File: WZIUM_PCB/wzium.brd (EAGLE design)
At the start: 160 x 100 mm, 15 parts, among them J1 RASPBERRYPI-40-PIN-GPIO_PTH

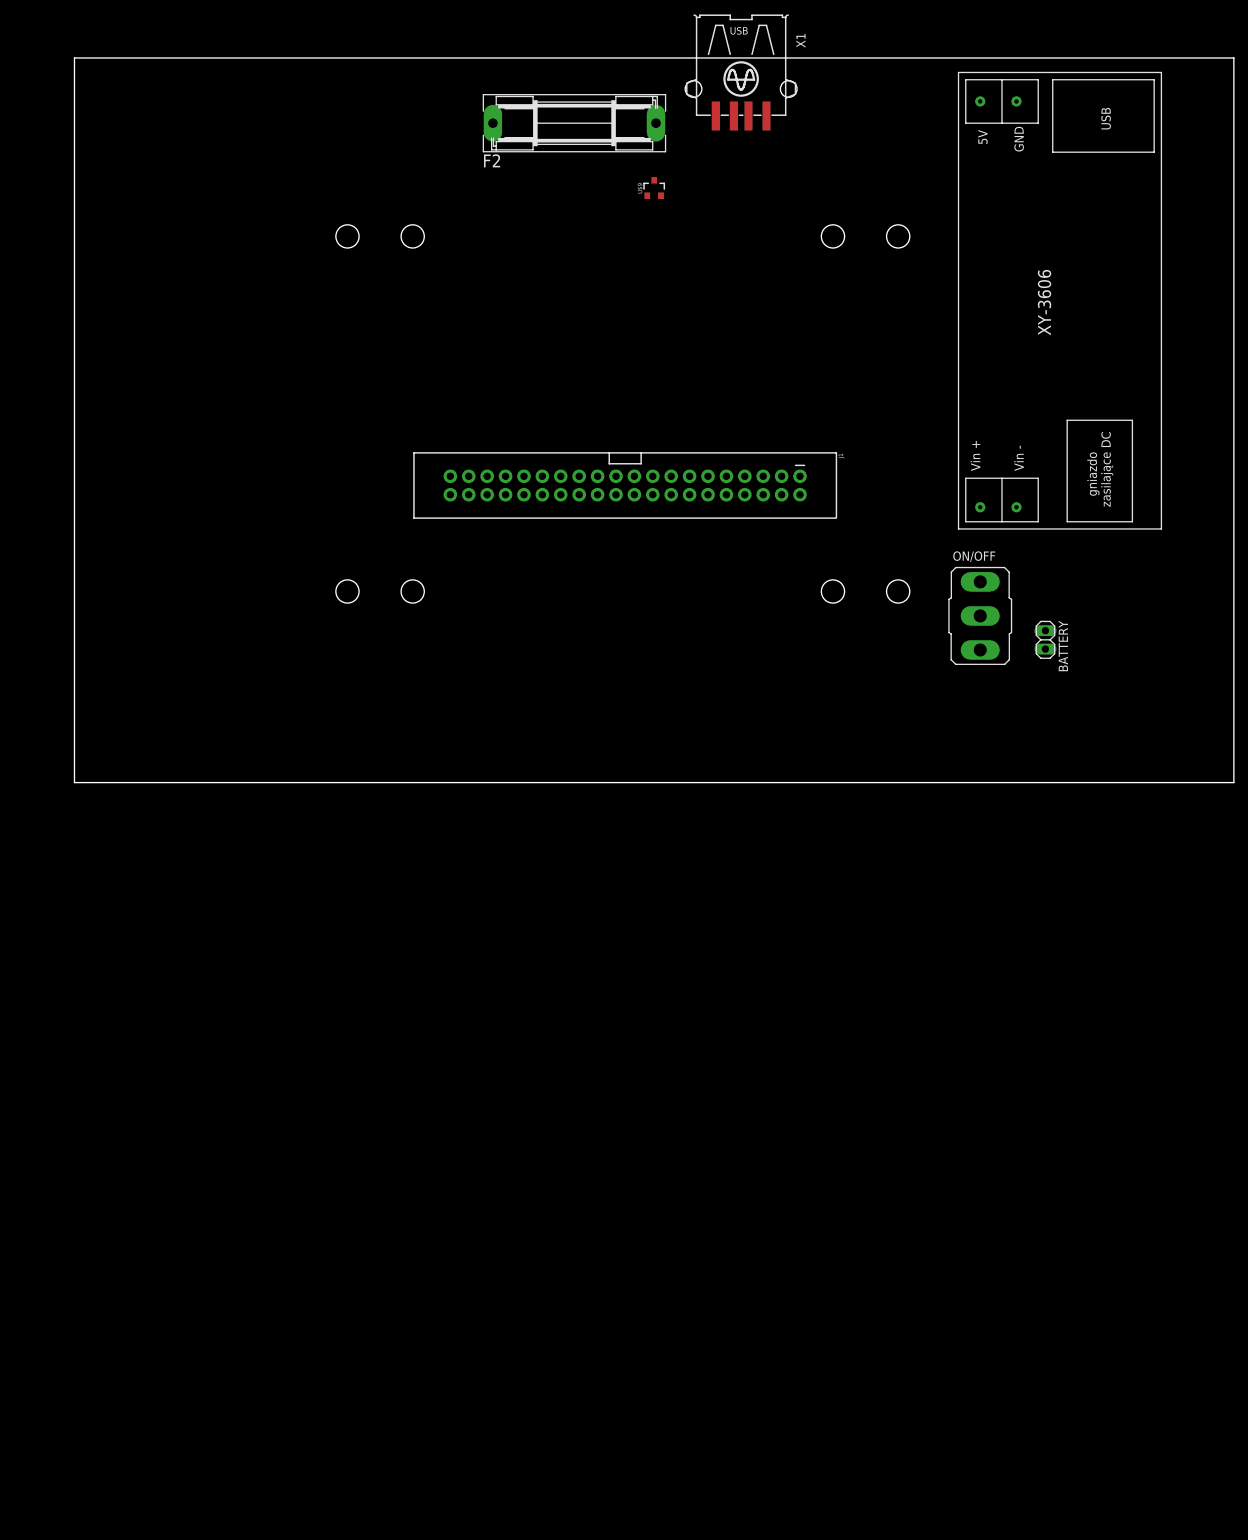
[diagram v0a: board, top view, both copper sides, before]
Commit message: [PCB] Zmieniono wielkość płytki na 10x10
Docelowo myślimy o JLC PCB, więc przeanalizowałem ich ceny:
-> 2.2 $ za płytkę 10x10 cm
-> 8.8 $ za płytkę 10x12 cm
Spróbujmy zmieścić się na płytce 10x10. Jeśli to niemożliwe to zmienimy rozmiar. Duże moduły można zamontować na podwoziu obok płytki ze sterownikiem i połączyć kablami.
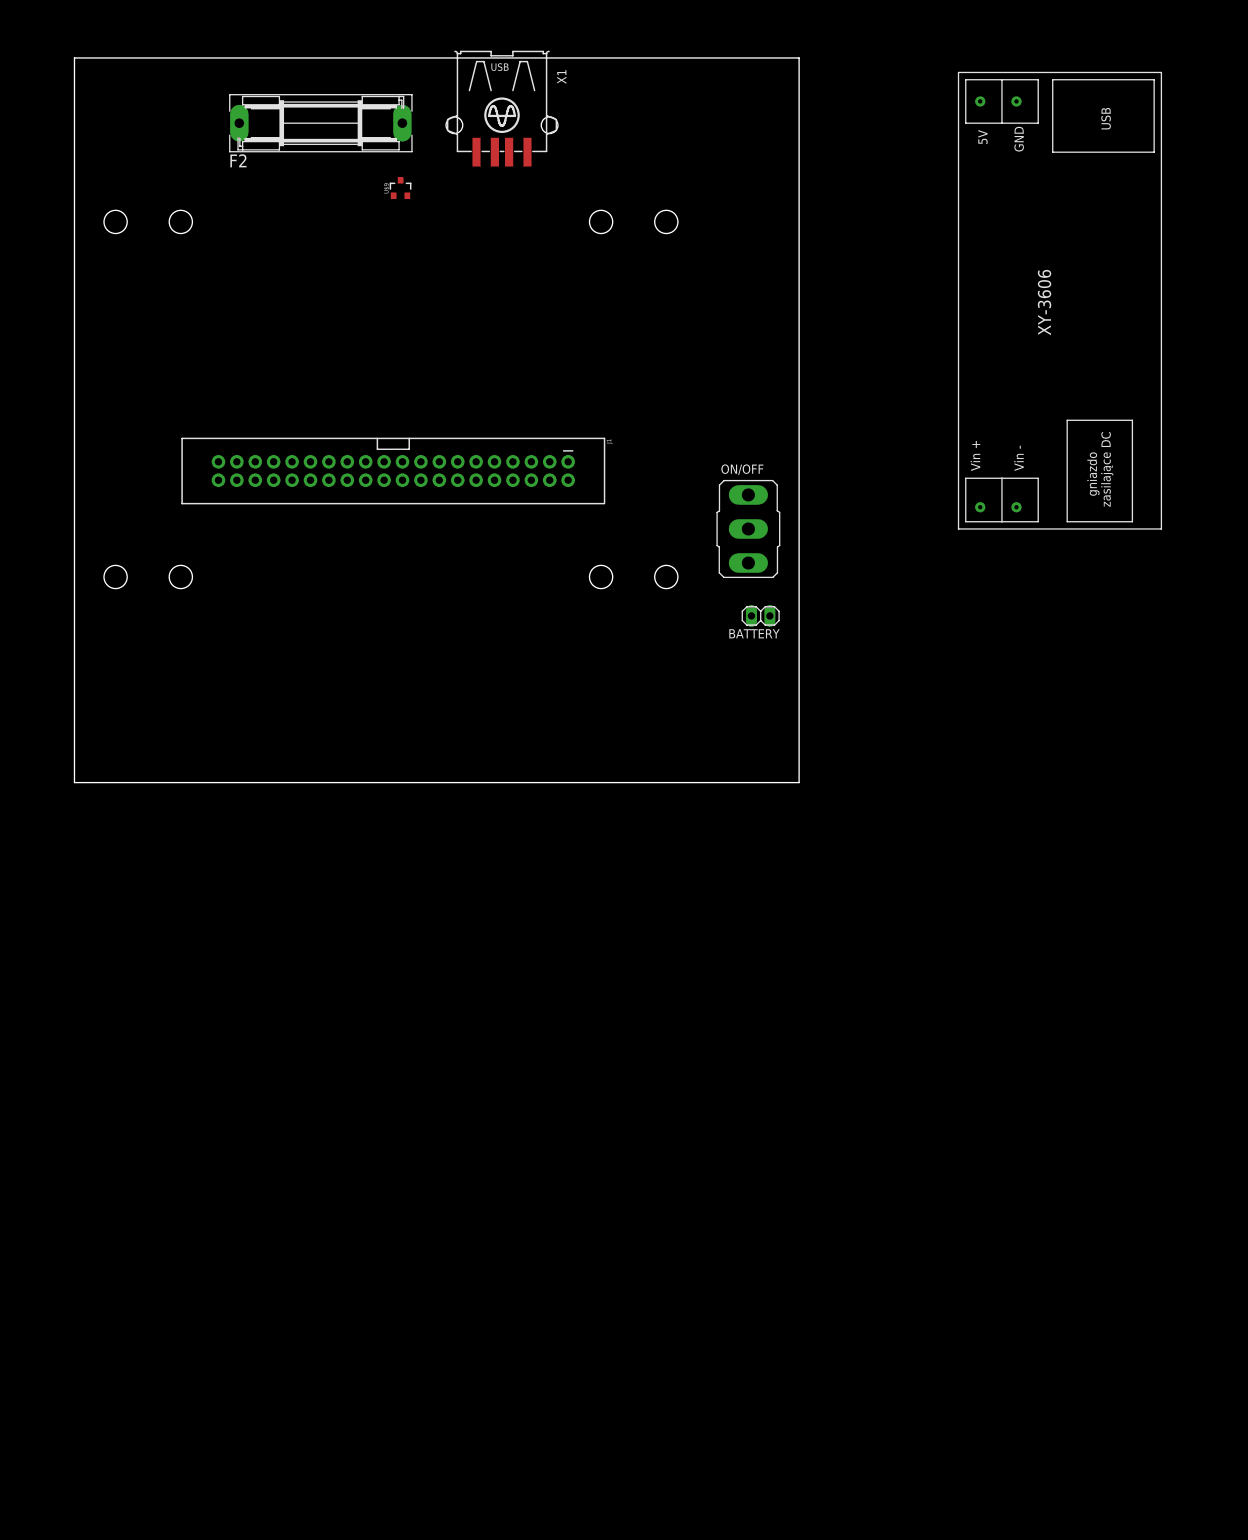
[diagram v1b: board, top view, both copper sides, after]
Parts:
- moved BATTERY 39.4 mm to (94.7, 23.0), turned to 180 degrees
- moved F2 35.0 mm to (34.0, 91.0)
- moved U$9 35.0 mm to (45.0, 82.0)
- moved ON/OFF 34.2 mm to (93.0, 35.0)
- moved X1 33.4 mm to (59.0, 101.0)
- moved J1 32.1 mm to (44.0, 43.0)
- moved U$3 32.1 mm to (72.7, 77.4)
- moved U$4 32.1 mm to (72.7, 28.4)
- moved U$7 32.1 mm to (81.7, 28.4)
- moved U$8 32.1 mm to (81.7, 77.4)
- moved U$1 32.1 mm to (14.7, 28.4)
- moved U$2 32.1 mm to (14.7, 77.4)
- moved U$5 32.1 mm to (5.67, 28.4)
- moved U$6 32.1 mm to (5.67, 77.4)
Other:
- board size 160 x 100 mm -> 100 x 100 mm

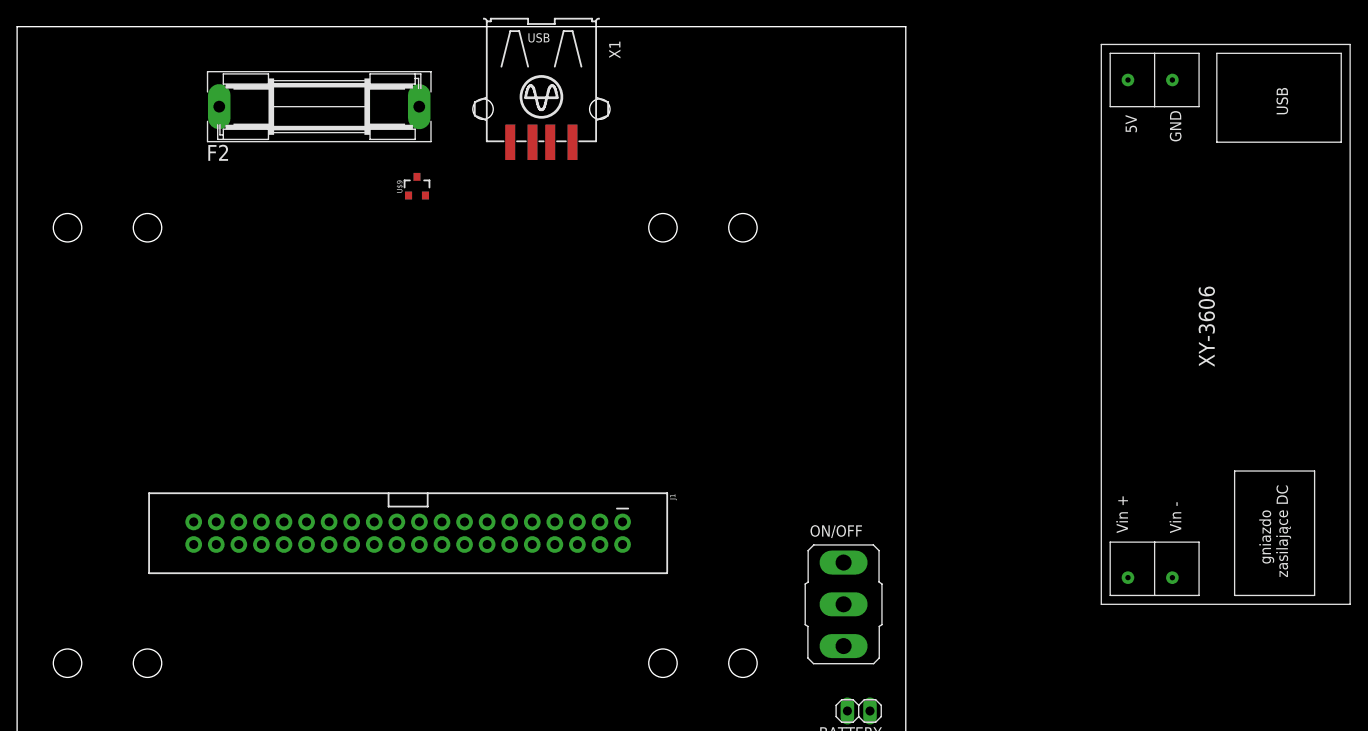
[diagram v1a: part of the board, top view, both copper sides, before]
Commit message: [PCB] Upgraded to EAGLE 9.6.2 i dodano biblioteki
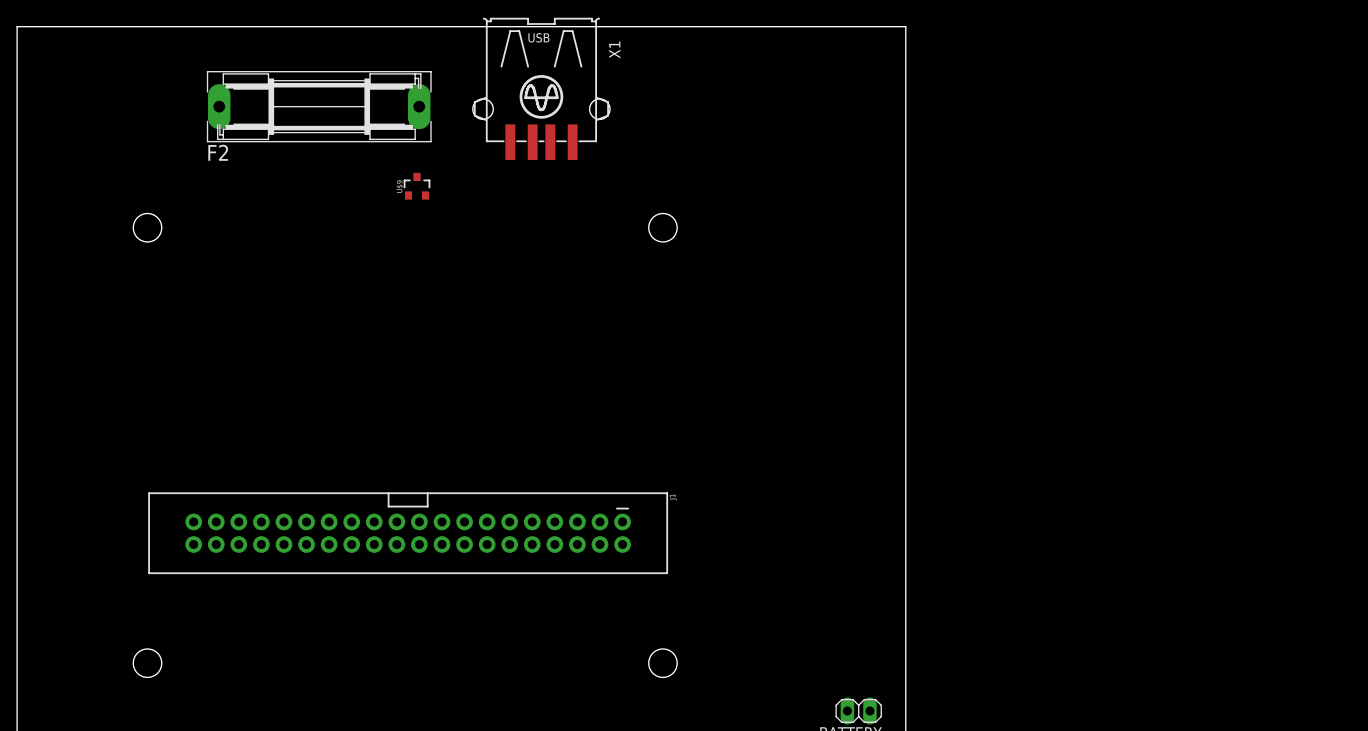
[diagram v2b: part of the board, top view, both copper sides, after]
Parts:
- removed ON/OFF: (no value), gm-switches:M9040P
- removed U$10: XY-3606, _MY_voltage_converters:CONVERTER_DC_TO_5V_DC
- removed U$2, U$6, U$7, U$8: (no value), WingTechCorner:M3-HOLE
- U$1, U$3, U$4, U$5: device WingTechCorner:M3-HOLE -> _MOUNTING_HOLES:M3-HOLE
- moved U$1 58.0 mm to (72.7, 28.4)
- moved U$3 58.0 mm to (14.7, 77.4)
- moved U$4 49.0 mm to (72.7, 77.4)
- moved U$5 9.00 mm to (14.7, 28.4)
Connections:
- removed net N$1: BATTERY.2, ON/OFF.3
- net 5V: no longer U$10.P$3
- net 6V: now also BATTERY.2; no longer ON/OFF.2, U$10.P$1
- net GND: no longer U$10.P$2, U$10.P$4
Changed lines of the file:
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@@
 <?xml version="1.0" encoding="utf-8"?>
 <!DOCTYPE eagle SYSTEM "eagle.dtd">
-<eagle version="9.4.2">
+<eagle version="9.6.2">
 <drawing>
 <settings>
@@
 <wire x1="100" y1="100" x2="0" y2="100" width="0" layer="20"/>
 <wire x1="0" y1="100" x2="0" y2="0" width="0" layer="20"/>
-<dimension x1="8.675" y1="28.3" x2="11.675" y2="28.3" x3="10.175" y3="17.325" textsize="0.3048" layer="1" dtype="horizontal" width="0.05"/>
-<dimension x1="13.075" y1="28.325" x2="16.275" y2="28.325" x3="14.675" y3="17.375" textsize="0.3048" layer="1" dtype="horizontal" width="0.05"/>
-<dimension x1="16.275" y1="28.375" x2="71.075" y2="28.45" x3="43.675" y3="23" textsize="0.4064" layer="1" dtype="horizontal" width="0.05"/>
-<dimension x1="14.675" y1="28.375" x2="72.675" y2="28.4" x3="43.675" y3="20" textsize="0.4064" layer="1" dtype="horizontal" width="0.05"/>
-<dimension x1="14.675" y1="77.375" x2="14.725" y2="28.375" x3="-2" y3="52.875" textsize="0.4064" layer="1" dtype="vertical" width="0.05"/>
-<dimension x1="5.675" y1="75.775" x2="5.675" y2="30.075" x3="1" y3="52.925" textsize="0.4064" layer="1" dtype="vertical" width="0.05"/>
+<dimension x1="17.675" y1="28.3" x2="11.675" y2="28.3" x3="14.675" y3="14.325" textsize="0.6096" layer="1" dtype="horizontal" width="0.05"/>
+<dimension x1="13.075" y1="28.325" x2="16.275" y2="28.325" x3="14.675" y3="17.375" textsize="0.6096" layer="1" dtype="horizontal" width="0.05"/>
+<dimension x1="16.275" y1="28.375" x2="71.075" y2="28.45" x3="43.675" y3="23" textsize="0.6096" layer="1" dtype="horizontal" width="0.05"/>
+<dimension x1="14.675" y1="28.375" x2="72.675" y2="28.4" x3="43.675" y3="20" textsize="0.6096" layer="1" dtype="horizontal" width="0.05"/>
+<dimension x1="14.675" y1="77.375" x2="14.725" y2="28.375" x3="-2" y3="52.875" textsize="1.016" layer="1" dtype="vertical" width="0.05"/>
+<dimension x1="14.8" y1="75.775" x2="14.7" y2="29.975" x3="2" y3="52.875" textsize="1.016" layer="1" dtype="vertical" width="0.05"/>
 </plain>
 <attributes>
@@
 </autorouter>
 <elements>
-<element name="U$1" library="WingTechCorner" package="M3-HOLE" value="" x="14.675" y="28.375" smashed="yes"/>
-<element name="U$2" library="WingTechCorner" package="M3-HOLE" value="" x="14.675" y="77.375" smashed="yes"/>
-<element name="U$3" library="WingTechCorner" package="M3-HOLE" value="" x="72.675" y="77.375" smashed="yes"/>
-<element name="U$4" library="WingTechCorner" package="M3-HOLE" value="" x="72.675" y="28.375" smashed="yes"/>
 <element name="J1" library="SparkFun-Connectors" library_urn="urn:adsk.eagle:library:513" package="2X20_SHROUDED" package3d_urn="urn:adsk.eagle:package:38279/1" value="RASPBERRYPI-40-PIN-GPIO_PTH" x="44" y="43" smashed="yes" rot="R270">
 <attribute name="NAME" x="73.464" y="47.445" size="0.6096" layer="25" font="vector" ratio="20" rot="R270"/>
@@
 <attribute name="VALUE" x="13.901" y="47.318" size="0.6096" layer="27" font="vector" ratio="20" rot="R270"/>
 </element>
-<element name="U$5" library="WingTechCorner" package="M3-HOLE" value="" x="5.675" y="28.375" smashed="yes"/>
-<element name="U$6" library="WingTechCorner" package="M3-HOLE" value="" x="5.675" y="77.375" smashed="yes"/>
-<element name="U$7" library="WingTechCorner" package="M3-HOLE" value="" x="81.675" y="28.375" smashed="yes"/>
-<element name="U$8" library="WingTechCorner" package="M3-HOLE" value="" x="81.675" y="77.375" smashed="yes"/>
 <element name="X1" library="con-yamaichi" library_urn="urn:adsk.eagle:library:202" package="USB-A003" package3d_urn="urn:adsk.eagle:package:11805/1" value="" x="59" y="101" smashed="yes" rot="R180">
 <attribute name="MF" value="" x="59" y="101" size="1.778" layer="27" rot="R180" display="off"/>
@@
 <attribute name="VALUE" x="97.24" y="26.175" size="1.27" layer="27" rot="R180"/>
 </element>
-<element name="ON/OFF" library="gm-switches" package="M9040P" value="" x="93" y="35" smashed="yes">
-<attribute name="NAME" x="89.19" y="42.62" size="1.27" layer="25" ratio="10"/>
-<attribute name="VALUE" x="89.19" y="25.475" size="1.27" layer="27" ratio="10"/>
-</element>
-<element name="U$10" library="_MY_voltage_converters" package="CONVERTER_DC_TO_5V_DC" value="XY-3606" x="150" y="35" smashed="yes" rot="R90"/>
+<element name="U$5" library="_MOUNTING_HOLES" package="M3-HOLE" value="" x="14.675" y="28.375" smashed="yes"/>
+<element name="U$1" library="_MOUNTING_HOLES" package="M3-HOLE" value="" x="72.675" y="28.375" smashed="yes"/>
+<element name="U$4" library="_MOUNTING_HOLES" package="M3-HOLE" value="" x="72.675" y="77.375" smashed="yes"/>
+<element name="U$3" library="_MOUNTING_HOLES" package="M3-HOLE" value="" x="14.675" y="77.375" smashed="yes"/>
 </elements>
 <signals>
@@
 <contactref element="U$9" pad="1"/>
 <contactref element="BATTERY" pad="1"/>
-<contactref element="U$10" pad="P$2"/>
 <contactref element="X1" pad="1"/>
-<contactref element="U$10" pad="P$4"/>
-<wire x1="57.97" y1="44.27" x2="62.5" y2="87" width="0" layer="19" extent="1-1"/>
-<wire x1="63.05" y1="41.73" x2="57.97" y2="44.27" width="0" layer="19" extent="1-1"/>
-<wire x1="52.89" y1="41.73" x2="57.97" y2="44.27" width="0" layer="19" extent="1-1"/>
-<wire x1="45.27" y1="41.73" x2="52.89" y2="41.73" width="0" layer="19" extent="1-1"/>
-<wire x1="37.65" y1="44.27" x2="45.27" y2="41.73" width="0" layer="19" extent="1-1"/>
+<wire x1="44.05" y1="81" x2="62.5" y2="87" width="0" layer="19" extent="1-1"/>
+<wire x1="37.65" y1="44.27" x2="44.05" y2="81" width="0" layer="19" extent="1-1"/>
 <wire x1="32.57" y1="41.73" x2="37.65" y2="44.27" width="0" layer="19" extent="1-1"/>
 <wire x1="27.49" y1="41.73" x2="32.57" y2="41.73" width="0" layer="19" extent="1-1"/>
+<wire x1="45.27" y1="41.73" x2="37.65" y2="44.27" width="0" layer="19" extent="1-1"/>
+<wire x1="52.89" y1="41.73" x2="45.27" y2="41.73" width="0" layer="19" extent="1-1"/>
+<wire x1="57.97" y1="44.27" x2="52.89" y2="41.73" width="0" layer="19" extent="1-1"/>
+<wire x1="63.05" y1="41.73" x2="57.97" y2="44.27" width="0" layer="19" extent="1-1"/>
 <wire x1="19.87" y1="44.27" x2="27.49" y2="41.73" width="0" layer="19" extent="1-1"/>
-<wire x1="130" y1="94" x2="27.49" y2="41.73" width="0" layer="19" extent="1-1"/>
-<wire x1="95.97" y1="23" x2="130" y2="94" width="0" layer="19" extent="1-1"/>
-<wire x1="130" y1="38" x2="95.97" y2="23" width="0" layer="19" extent="1-1"/>
-<wire x1="44.05" y1="81" x2="130" y2="38" width="0" layer="19" extent="1-1"/>
+<wire x1="95.97" y1="23" x2="63.05" y2="41.73" width="0" layer="19" extent="1-1"/>
 </signal>
 <signal name="5V">
 <contactref element="J1" pad="4"/>
 <contactref element="J1" pad="2"/>
-<contactref element="U$10" pad="P$3"/>
 <contactref element="F2" pad="1"/>
-<wire x1="65.59" y1="41.73" x2="68.13" y2="41.73" width="0" layer="19" extent="1-1"/>
-<wire x1="125" y1="94" x2="65.59" y2="41.73" width="0" layer="19" extent="1-1"/>
-<wire x1="22.7478" y1="91" x2="125" y2="94" width="0" layer="19" extent="1-1"/>
+<wire x1="65.59" y1="41.73" x2="22.7478" y2="91" width="0" layer="19" extent="1-1"/>
+<wire x1="68.13" y1="41.73" x2="65.59" y2="41.73" width="0" layer="19" extent="1-1"/>
 </signal>
 <signal name="VIN">
@@
 </signal>
 <signal name="6V">
-<contactref element="ON/OFF" pad="2"/>
-<contactref element="U$10" pad="P$1"/>
-<wire x1="125" y1="38" x2="93" y2="35" width="0" layer="19" extent="1-1"/>
-</signal>
-<signal name="N$1">
 <contactref element="BATTERY" pad="2"/>
-<contactref element="ON/OFF" pad="3"/>
-<wire x1="93.43" y1="23" x2="93" y2="30.301" width="0" layer="19" extent="1-1"/>
 </signal>
 </signals>
@@
 </drawing>
 <compatibility>
-<note version="6.3" minversion="6.2.2" severity="warning">
-Since Version 6.2.2 text objects can contain more than one line,
-which will not be processed correctly with this version.
-</note>
 <note version="8.2" severity="warning">
 Since Version 8.2, EAGLE supports online libraries. The ids
